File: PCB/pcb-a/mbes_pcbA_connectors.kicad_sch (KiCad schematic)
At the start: 14 parts, among them J1 Conn_02x05_Counter_Clockwise, J2 Conn_02x04_Counter_Clockwise, U3 L7805

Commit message: Fixes
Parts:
- removed J2: Conn_02x04_Counter_Clockwise, Connector_PinHeader_2.54mm:PinHeader_2x04_P2.54mm_Vertical, symbol Connector_Generic:Conn_02x04_Counter_Clockwise
- added J2: Conn_02x05_Counter_Clockwise, Connector_PinHeader_2.54mm:PinHeader_2x05_P2.54mm_Vertical, symbol Connector_Generic:Conn_02x05_Counter_Clockwise
- added clutch_sw1: Conn_01x02, Connector_Wire:SolderWire-0.75sqmm_1x02_P4.8mm_D1.25mm_OD2.3mm, symbol Connector_Generic:Conn_01x02
- Decomp_1, LightOnOff_sw1, addLights1, powerOFF1: footprint Connector_Wire:SolderWire-0.15sqmm_1x02_P4mm_D0.5mm_OD1.5mm -> Connector_Wire:SolderWire-0.75sqmm_1x02_P4.8mm_D1.25mm_OD2.3mm
- extpwr1: footprint Connector_PinHeader_2.54mm:PinHeader_1x02_P2.54mm_Vertical -> Connector_Wire:SolderWire-0.75sqmm_1x02_P4.8mm_D1.25mm_OD2.3mm
- rightCtrls_conn1: footprint Connector_Wire:SolderWire-0.15sqmm_1x06_P4mm_D0.5mm_OD1.5mm -> Connector_Wire:SolderWire-0.25sqmm_1x06_P4.2mm_D0.65mm_OD1.7mm
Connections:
- net GND: now also clutch_sw1.1 (Pin_1)
- net c_engineOFF: now also J2.7 (Pin_7)
- net c_leftArrow: now also J2.3 (Pin_3)
- net c_rightArrow: now also J2.2 (Pin_2)
- net o_engineON: now also J2.4 (Pin_4)
- net o_engineReady: now also J2.8 (Pin_8)
- net o_keepAlive: now also J2.9 (Pin_9)
- net o_neutral: now also J2.10 (Pin_10)
- new net i_clutch: clutch_sw1.2 (Pin_2)
- no-connect marks 2 -> 4

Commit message: Fixes and changes
- 8pin pin-header connectors have been replaced with more standard 10pin connectors
- Wrong components sizes have been fixed
- too small solder-wire connectors have been fixed
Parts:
- leftCtrls_conn1, rightCtrls_conn1: footprint Connector_Wire:SolderWire-0.25sqmm_1x06_P4.2mm_D0.65mm_OD1.7mm -> Custom_conn_wire:SolderWire-0.25sqmm_1x06_P4.2mm_D1.0mm_OD2.2mm
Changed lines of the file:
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@@
 (kicad_sch
-	(version 20231120)
+	(version 20250114)
 	(generator "eeschema")
-	(generator_version "8.0")
+	(generator_version "9.0")
 	(paper "A4")
 	(title_block
@@
 		(company "Panicosoft")
 	)
+	(text "1) Start butt. (orange)\n2) GND (blue)\n3) Brake sw. (light blue)\n4) Start butt. (black/white)\n5) Engine OFF (black)\n6) Engine ON (yellow/black)"
+		(exclude_from_sim no)
+		(at 25.4 66.04 0)
+		(effects
+			(font
+				(size 1.27 1.27)
+			)
+			(justify left bottom)
+		)
+	)
+	(text "1) GND (gray)\n2) Left arrow (light blue)\n3) DOWN light (white)\n4) UP Light (blue)\n5) Right Arrow (orange)\n6) Horn (verde)"
+		(exclude_from_sim no)
+		(at 28.067 90.932 0)
+		(effects
+			(font
+				(size 1.27 1.27)
+			)
+			(justify left bottom)
+		)
+	)
+	(text "1) Rear light\n2) Left arrow\n3) Right arrow\n4) NC\n5) Rear brake\n6) START relay\n7) Neutral gear\n8) Eng-off CDI"
+		(exclude_from_sim no)
+		(at 157.226 67.31 0)
+		(effects
+			(font
+				(size 1.27 1.27)
+			)
+			(justify left bottom)
+		)
+	)
 	(junction
 		(at 65.786 116.84)
@@
 		)
 	)
-	(text "1) Start butt. (orange)\n2) GND (blue)\n3) Brake sw. (light blue)\n4) Start butt. (black/white)\n5) Engine OFF (black)\n6) Engine ON (yellow/black)"
-		(exclude_from_sim no)
-		(at 25.4 66.04 0)
-		(effects
-			(font
-				(size 1.27 1.27)
-			)
-			(justify left bottom)
-		)
-	)
-	(text "1) GND (gray)\n2) Left arrow (light blue)\n3) DOWN light (white)\n4) UP Light (blue)\n5) Right Arrow (orange)\n6) Horn (verde)"
-		(exclude_from_sim no)
-		(at 28.067 90.932 0)
-		(effects
-			(font
-				(size 1.27 1.27)
-			)
-			(justify left bottom)
-		)
-	)
-	(text "1) Rear light\n2) Left arrow\n3) Right arrow\n4) NC\n5) Rear brake\n6) START relay\n7) Neutral gear\n8) Eng-off CDI"
-		(exclude_from_sim no)
-		(at 157.226 67.31 0)
-		(effects
-			(font
-				(size 1.27 1.27)
-			)
-			(justify left bottom)
-		)
-	)
 	(global_label "o_engineReady"
 		(shape input)
@@
 			)
 		)
-		(property "Footprint" "Connector_Wire:SolderWire-0.25sqmm_1x06_P4.2mm_D0.65mm_OD1.7mm"
+		(property "Footprint" "Custom_conn_wire:SolderWire-0.25sqmm_1x06_P4.2mm_D1.0mm_OD2.2mm"
 			(at 56.642 83.312 0)
 			(effects
@@
 			)
 		)
-		(property "Footprint" "Connector_Wire:SolderWire-0.25sqmm_1x06_P4.2mm_D0.65mm_OD1.7mm"
+		(property "Footprint" "Custom_conn_wire:SolderWire-0.25sqmm_1x06_P4.2mm_D1.0mm_OD2.2mm"
 			(at 56.642 58.42 0)
 			(effects

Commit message: Small fixes...
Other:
- note added: "1) Rear light 2) Left arrow light 3) Right arrow light 4) Byke stand switch 5) Rear brake switch 6) START relay 7) Neutral gear switch 8) Eng-off CDI"
- note removed: "1) Rear light 2) Left arrow 3) Right arrow 4) NC 5) Rear brake 6) START relay 7) Neutral gear 8) Eng-off CDI"
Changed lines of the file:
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@@
 		)
 	)
-	(text "1) Rear light\n2) Left arrow\n3) Right arrow\n4) NC\n5) Rear brake\n6) START relay\n7) Neutral gear\n8) Eng-off CDI"
+	(text "1) Rear light\n2) Left arrow light\n3) Right arrow light\n4) Byke stand switch\n5) Rear brake switch\n6) START relay\n7) Neutral gear switch\n8) Eng-off CDI"
 		(exclude_from_sim no)
-		(at 157.226 67.31 0)
+		(at 151.638 65.024 0)
 		(effects
 			(font

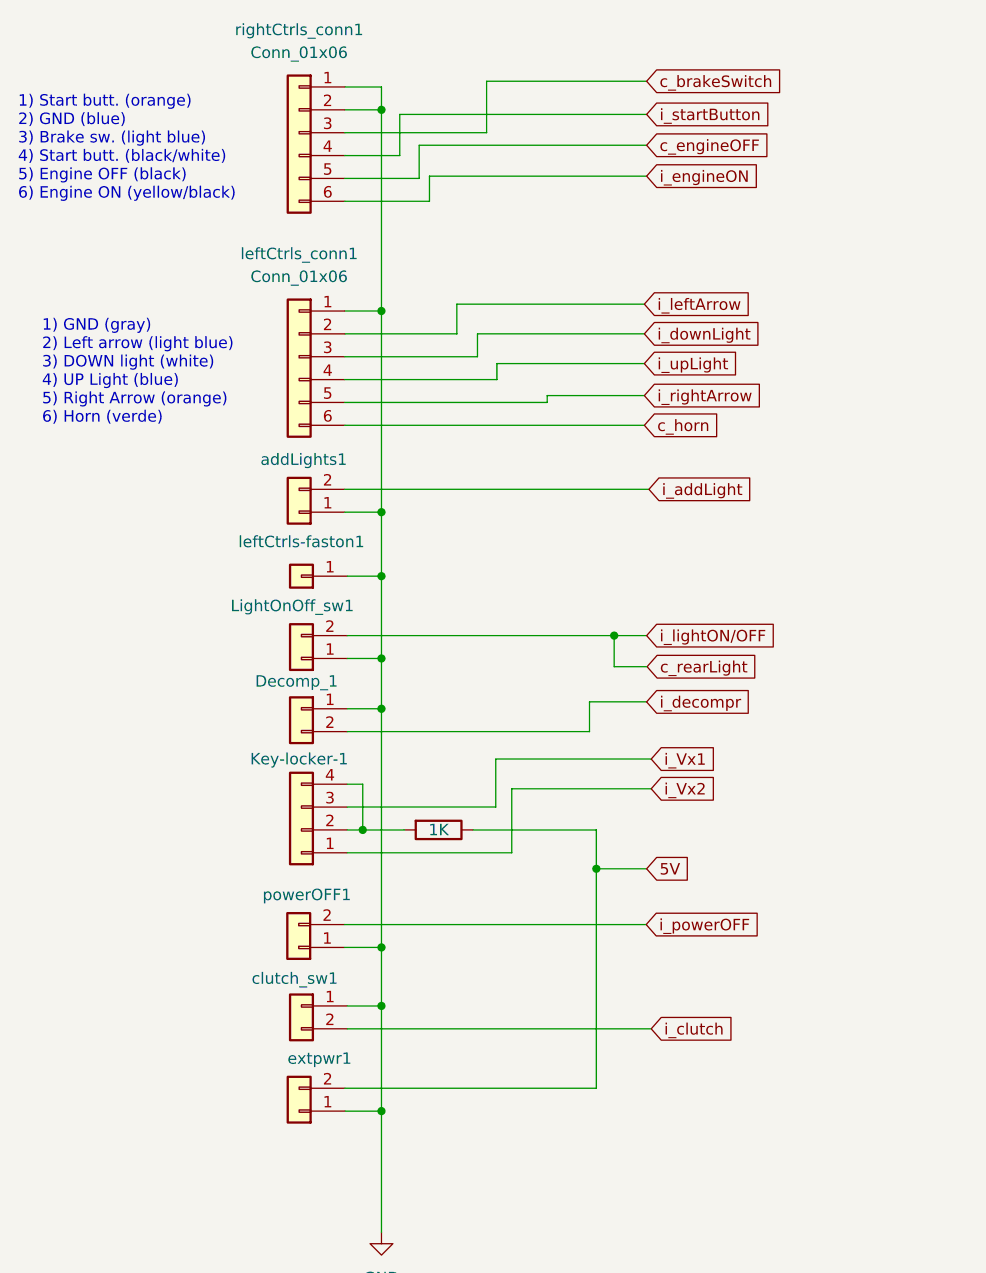
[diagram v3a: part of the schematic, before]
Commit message: Wires to welded has been substituted bt pin-header connectors
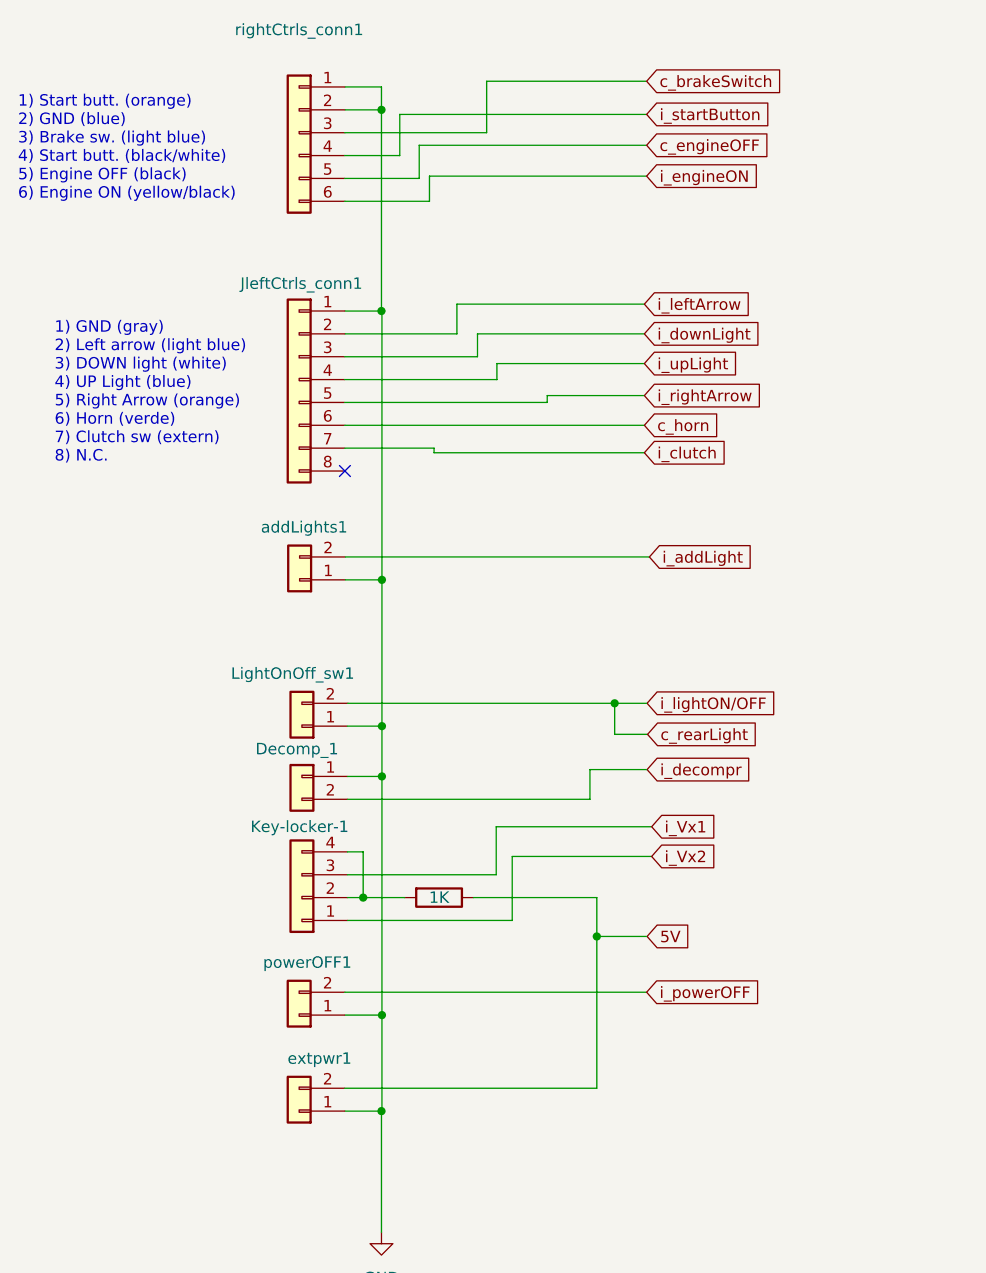
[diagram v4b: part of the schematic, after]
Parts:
- removed clutch_sw1: Conn_01x02, Connector_Wire:SolderWire-0.75sqmm_1x02_P4.8mm_D1.25mm_OD2.3mm, symbol Connector_Generic:Conn_01x02
- removed leftCtrls-faston1: Conn_01x01, Connector_Wire:SolderWire-0.5sqmm_1x01_D0.9mm_OD2.1mm, symbol Connector_Generic:Conn_01x01
- removed leftCtrls_conn1: Conn_01x06, Custom_conn_wire:SolderWire-0.25sqmm_1x06_P4.2mm_D1.0mm_OD2.2mm, symbol Connector_Generic:Conn_01x06
- added JleftCtrls_conn1: Conn_01x08, Connector_PinHeader_2.54mm:PinHeader_1x08_P2.54mm_Vertical, symbol Connector_Generic:Conn_01x08
- Decomp_1, LightOnOff_sw1, addLights1, extpwr1, powerOFF1: footprint Connector_Wire:SolderWire-0.75sqmm_1x02_P4.8mm_D1.25mm_OD2.3mm -> Connector_PinHeader_2.54mm:PinHeader_1x02_P2.54mm_Vertical
- rightCtrls_conn1: footprint Custom_conn_wire:SolderWire-0.25sqmm_1x06_P4.2mm_D1.0mm_OD2.2mm -> Connector_PinHeader_2.54mm:PinHeader_1x06_P2.54mm_Vertical
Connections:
- net GND: now also JleftCtrls_conn1.1 (Pin_1)
- net c_horn: now also JleftCtrls_conn1.6 (Pin_6)
- net i_clutch: now also JleftCtrls_conn1.7 (Pin_7)
- net i_downLight: now also JleftCtrls_conn1.3 (Pin_3)
- net i_leftArrow: now also JleftCtrls_conn1.2 (Pin_2)
- net i_rightArrow: now also JleftCtrls_conn1.5 (Pin_5)
- net i_upLight: now also JleftCtrls_conn1.4 (Pin_4)
- no-connect marks 4 -> 5
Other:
- note added: "1) GND (gray) 2) Left arrow (light blue) 3) DOWN light (white) 4) UP Light (blue) 5) Right Arrow (orange) 6) Horn (verde) 7) Clutch sw (extern) 8) N.C."
- note removed: "1) GND (gray) 2) Left arrow (light blue) 3) DOWN light (white) 4) UP Light (blue) 5) Right Arrow (orange) 6) Horn (verde)"
- moved on the sheet: Decomp_1, Key-locker-1, LightOnOff_sw1, addLights1, powerOFF1

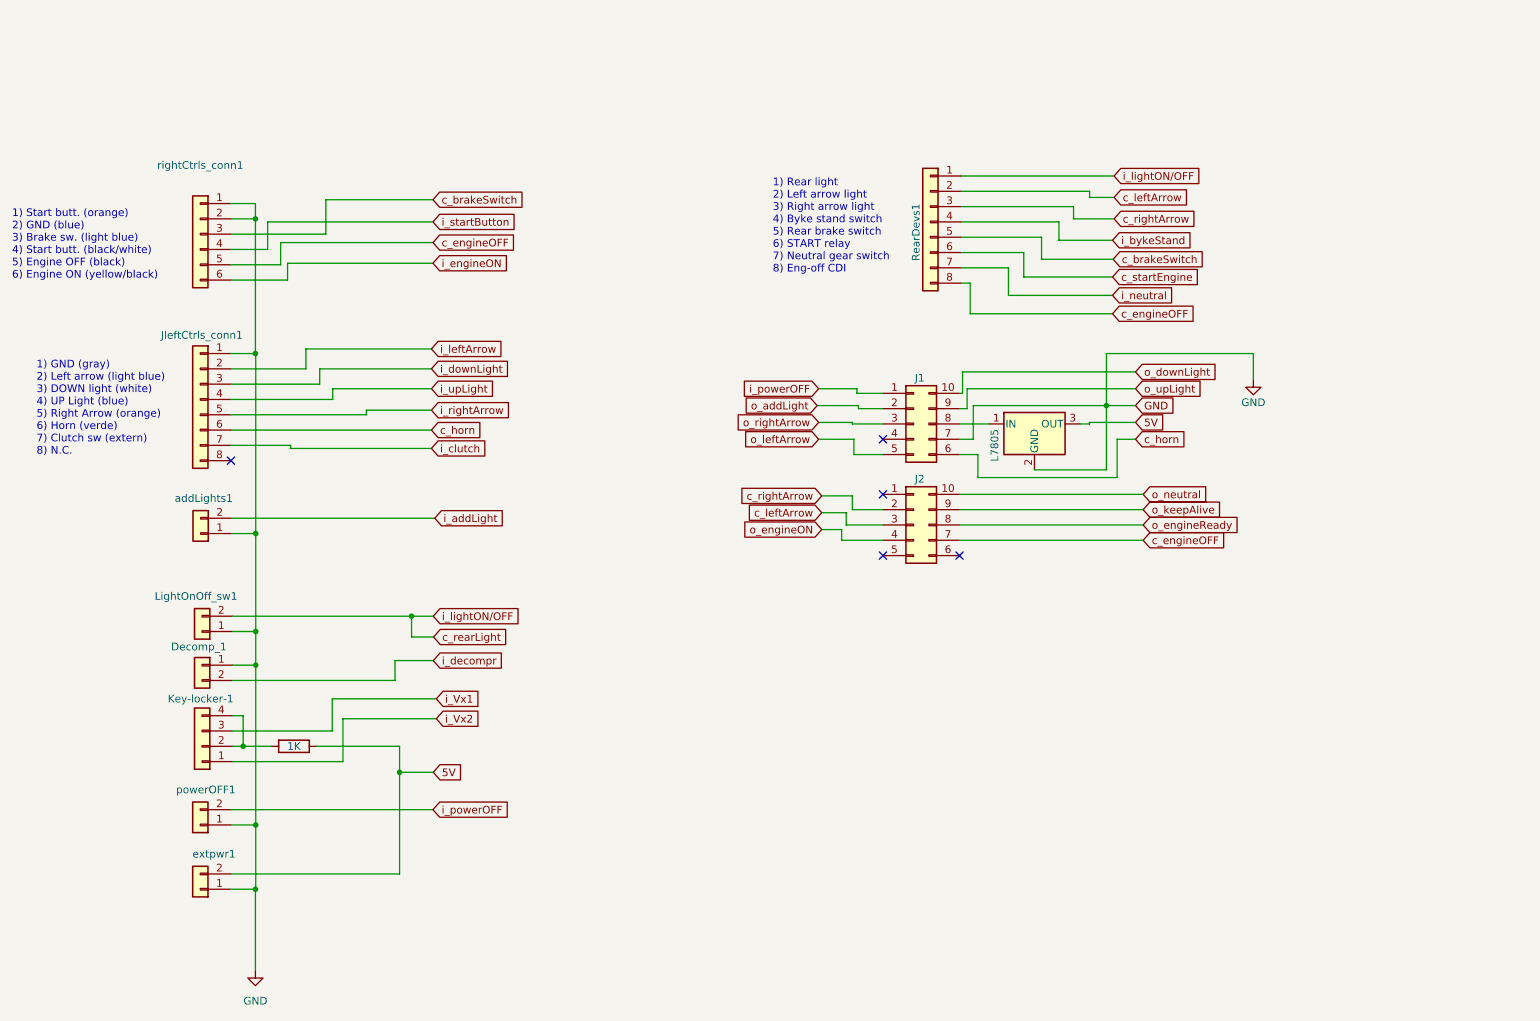
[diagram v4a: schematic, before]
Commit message: Communication with the rear power stage has been changed
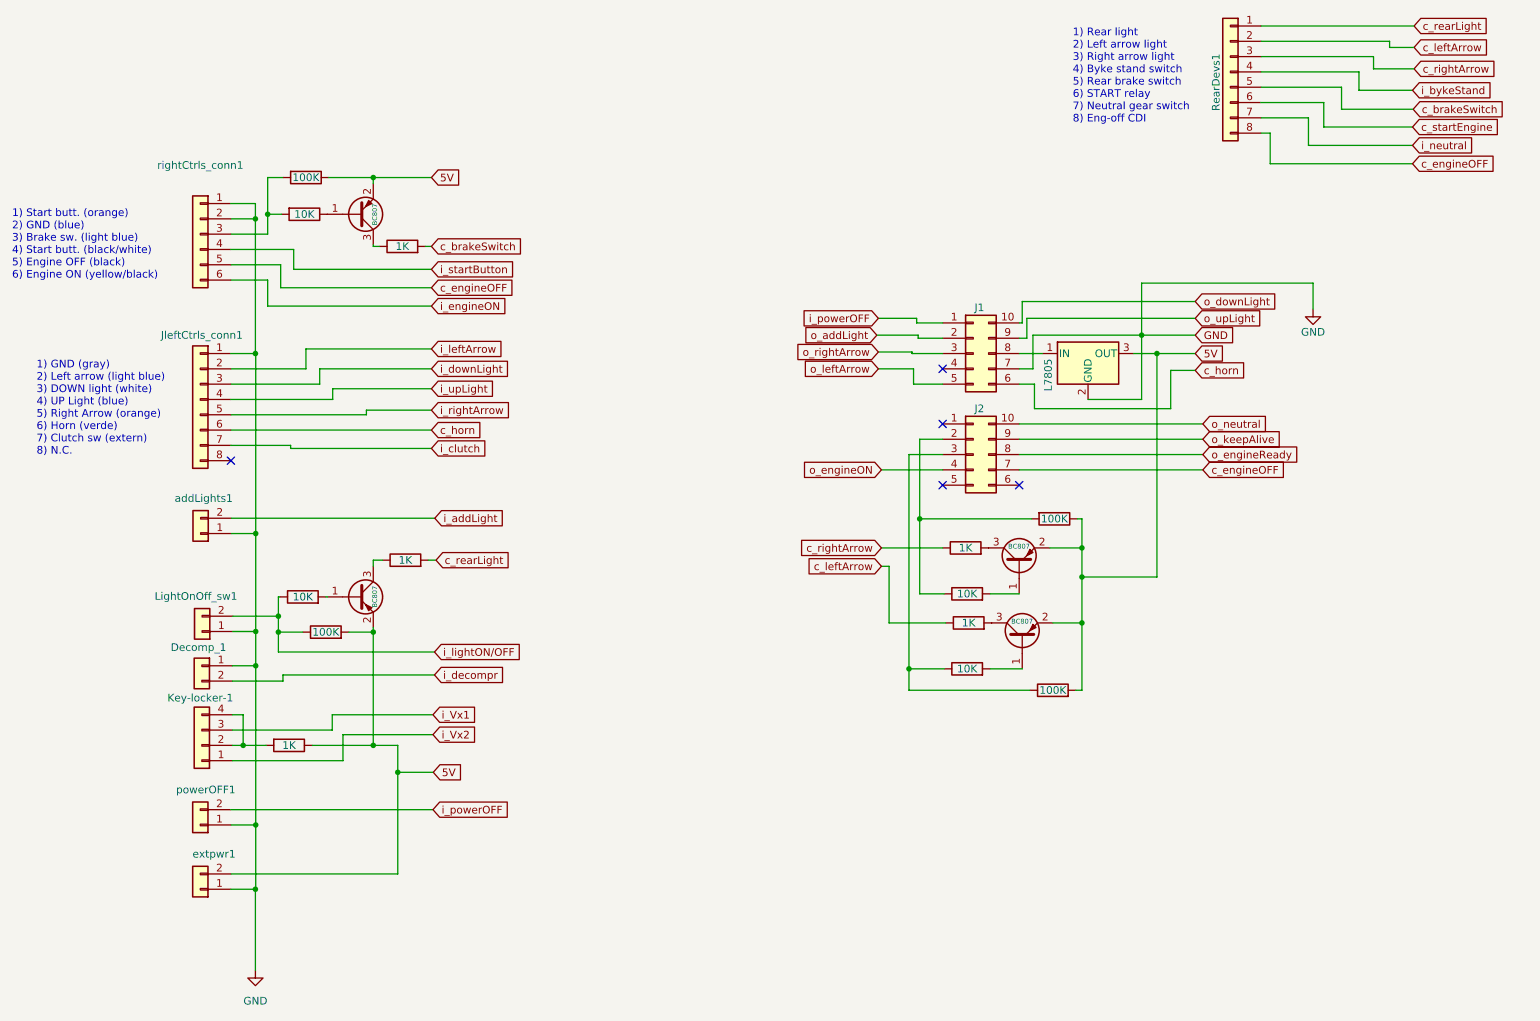
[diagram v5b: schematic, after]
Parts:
- added Q2, Q4, Q5, Q6: BC807, Package_TO_SOT_SMD:SOT-23, symbol Transistor_BJT:BC807
- added R11, R12, R13, R20: 1K, Resistor_SMD:R_1206_3216Metric, symbol Device:R
- added R14, R16, R17, R19: 100K, Resistor_SMD:R_1206_3216Metric, symbol Device:R
- added R18, R5, R8, R9: 10K, Resistor_SMD:R_1206_3216Metric, symbol Device:R
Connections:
- net 5V: now also Q2.2 (E), Q4.2 (E), Q5.2 (E), Q6.2 (E), R14.1, R16.1, R17.2, R19.2
- net c_brakeSwitch: now also R13.2; no longer rightCtrls_conn1.3 (Pin_3)
- net c_leftArrow: now also R11.1; no longer J2.3 (Pin_3)
- net c_rearLight: now also R20.2; no longer LightOnOff_sw1.2 (Pin_2)
- net c_rightArrow: now also R12.1; no longer J2.2 (Pin_2)
- new net: J2.3 (Pin_3), R17.1, R8.1
- new net: R14.2, R9.2, rightCtrls_conn1.3 (Pin_3)
- new net: Q6.1 (B), R18.2
- new net: Q6.3 (C), R20.1
- new net: Q4.1 (B), R8.2
- new net: J2.2 (Pin_2), R16.2, R5.1
- new net: Q4.3 (C), R11.2
- new net: Q5.1 (B), R9.1
- new net: Q5.3 (C), R13.1
- new net: Q2.3 (C), R12.2
- new net: Q2.1 (B), R5.2
- new net i_lightON/OFF: LightOnOff_sw1.2 (Pin_2), R18.1, R19.1
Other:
- moved on the sheet: J1, J2, RearDevs1
